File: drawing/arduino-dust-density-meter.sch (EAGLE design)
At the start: 7 parts

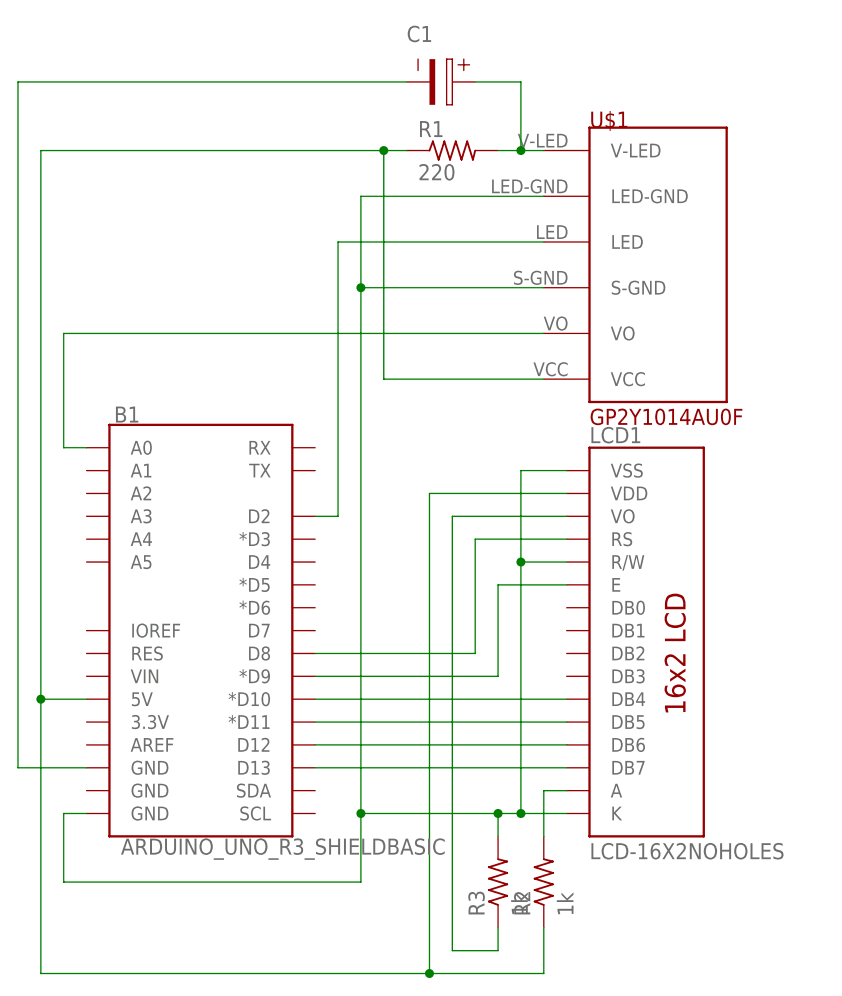
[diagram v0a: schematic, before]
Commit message: [DOCUMENT] Modify schematic for ease of viewing
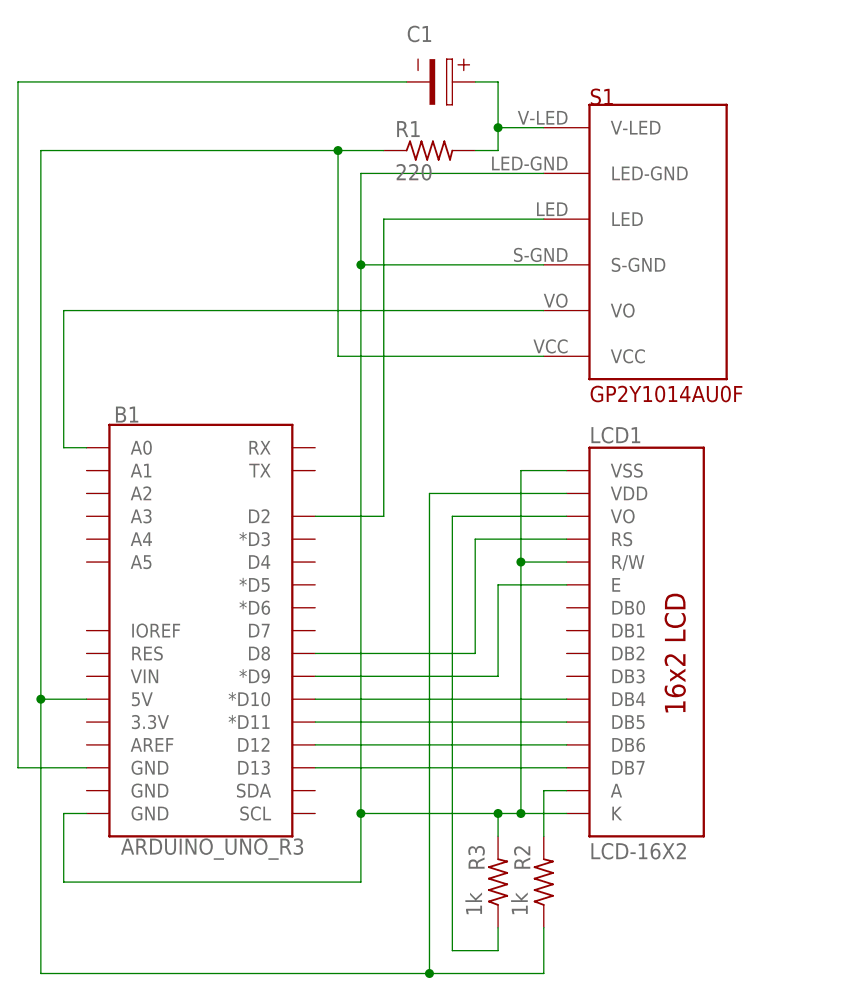
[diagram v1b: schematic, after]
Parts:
- removed U$1: GP2Y1014AU0F, sharp-dust-sensor:GP2Y1014AU0F
- added S1: GP2Y1014AU0F, sharp-dust-sensor:GP2Y1014AU0F
- B1: value ARDUINO_UNO_R3_SHIELDBASIC -> ARDUINO_UNO_R3
- LCD1: value LCD-16X2NOHOLES -> LCD-16X2
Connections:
- net N$1: now also S1.V-LED; no longer U$1.V-LED
- net N$2: now also S1.VCC; no longer U$1.VCC
- net N$4: now also S1.LED-GND, S1.S-GND; no longer U$1.LED-GND, U$1.S-GND
- net N$5: now also S1.LED; no longer U$1.LED
- net N$6: now also S1.VO; no longer U$1.VO
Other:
- moved on the sheet: R1
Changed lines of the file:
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@@
 </classes>
 <parts>
-<part name="B1" library="SparkFun-Boards" library_urn="urn:adsk.eagle:library:509" deviceset="ARDUINO_UNO_R3_SHIELD" device="BASIC" package3d_urn="urn:adsk.eagle:package:37321/1"/>
-<part name="U$1" library="sharp-dust-sensor" library_urn="urn:adsk.eagle:library:12467232" deviceset="GP2Y1014AU0F" device="" package3d_urn="urn:adsk.eagle:package:12467238/4"/>
+<part name="B1" library="SparkFun-Boards" library_urn="urn:adsk.eagle:library:509" deviceset="ARDUINO_UNO_R3_SHIELD" device="BASIC" package3d_urn="urn:adsk.eagle:package:37321/1" value="ARDUINO_UNO_R3"/>
+<part name="S1" library="sharp-dust-sensor" library_urn="urn:adsk.eagle:library:12467232" deviceset="GP2Y1014AU0F" device="" package3d_urn="urn:adsk.eagle:package:12467238/4"/>
 <part name="R1" library="BeagleBone_Black_Wireless" library_urn="urn:adsk.eagle:library:6644236" deviceset="R-US_" device="0309/12" package3d_urn="urn:adsk.eagle:package:8118473/1" value="220"/>
 <part name="C1" library="Wurth_Elektronik_Passive_Capacitors_rev18b" library_urn="urn:adsk.eagle:library:491551" deviceset="WCAP-PTG5" device="_870025575007" package3d_urn="urn:adsk.eagle:package:491745/2" technology="_10X12,5"/>
-<part name="LCD1" library="SparkFun-Displays" library_urn="urn:adsk.eagle:library:515" deviceset="LCD-16X2" device="NOHOLES" package3d_urn="urn:adsk.eagle:package:38513/1"/>
+<part name="LCD1" library="SparkFun-Displays" library_urn="urn:adsk.eagle:library:515" deviceset="LCD-16X2" device="NOHOLES" package3d_urn="urn:adsk.eagle:package:38513/1" value="LCD-16X2"/>
 <part name="R2" library="BeagleBone_Black_Wireless" library_urn="urn:adsk.eagle:library:6644236" deviceset="R-US_" device="0309/12" package3d_urn="urn:adsk.eagle:package:8118473/1" value="1k"/>
 <part name="R3" library="BeagleBone_Black_Wireless" library_urn="urn:adsk.eagle:library:6644236" deviceset="R-US_" device="0309/12" package3d_urn="urn:adsk.eagle:package:8118473/1" value="1k"/>
@@
 <attribute name="VALUE" x="105.41" y="12.446" size="1.778" layer="96" font="vector" align="top-left"/>
 </instance>
-<instance part="U$1" gate="G$1" x="165.1" y="76.2" smashed="yes">
-<attribute name="NAME" x="157.48" y="91.44" size="1.778" layer="94"/>
-<attribute name="VALUE" x="157.48" y="58.42" size="1.778" layer="94"/>
+<instance part="S1" gate="G$1" x="165.1" y="78.74" smashed="yes">
+<attribute name="NAME" x="157.48" y="93.98" size="1.778" layer="94"/>
+<attribute name="VALUE" x="157.48" y="60.96" size="1.778" layer="94"/>
 </instance>
-<instance part="R1" gate="G$1" x="142.24" y="88.9" smashed="yes">
-<attribute name="NAME" x="138.43" y="90.3986" size="1.778" layer="95"/>
-<attribute name="VALUE" x="138.43" y="85.598" size="1.778" layer="96"/>
+<instance part="R1" gate="G$1" x="139.7" y="88.9" smashed="yes">
+<attribute name="NAME" x="135.89" y="90.3986" size="1.778" layer="95"/>
+<attribute name="VALUE" x="135.89" y="85.598" size="1.778" layer="96"/>
 </instance>
 <instance part="C1" gate="G$1" x="139.7" y="96.52" smashed="yes" rot="R270">
@@
 </instance>
 <instance part="R2" gate="G$1" x="152.4" y="7.62" smashed="yes" rot="R90">
-<attribute name="NAME" x="150.9014" y="3.81" size="1.778" layer="95" rot="R90"/>
-<attribute name="VALUE" x="155.702" y="3.81" size="1.778" layer="96" rot="R90"/>
+<attribute name="NAME" x="150.9014" y="8.89" size="1.778" layer="95" rot="R90"/>
+<attribute name="VALUE" x="150.622" y="3.81" size="1.778" layer="96" rot="R90"/>
 </instance>
 <instance part="R3" gate="G$1" x="147.32" y="7.62" smashed="yes" rot="R90">
-<attribute name="NAME" x="145.8214" y="3.81" size="1.778" layer="95" rot="R90"/>
-<attribute name="VALUE" x="150.622" y="3.81" size="1.778" layer="96" rot="R90"/>
+<attribute name="NAME" x="145.8214" y="8.89" size="1.778" layer="95" rot="R90"/>
+<attribute name="VALUE" x="145.542" y="3.81" size="1.778" layer="96" rot="R90"/>
 </instance>
 </instances>
@@
 <net name="N$1" class="0">
 <segment>
+<pinref part="S1" gate="G$1" pin="V-LED"/>
+<wire x1="152.4" y1="91.44" x2="147.32" y2="91.44" width="0.1524" layer="91"/>
+<pinref part="C1" gate="G$1" pin="1"/>
+<wire x1="144.78" y1="96.52" x2="147.32" y2="96.52" width="0.1524" layer="91"/>
+<wire x1="147.32" y1="96.52" x2="147.32" y2="91.44" width="0.1524" layer="91"/>
 <pinref part="R1" gate="G$1" pin="2"/>
-<pinref part="U$1" gate="G$1" pin="V-LED"/>
-<wire x1="152.4" y1="88.9" x2="149.86" y2="88.9" width="0.1524" layer="91"/>
-<pinref part="C1" gate="G$1" pin="1"/>
-<wire x1="149.86" y1="88.9" x2="147.32" y2="88.9" width="0.1524" layer="91"/>
-<wire x1="144.78" y1="96.52" x2="149.86" y2="96.52" width="0.1524" layer="91"/>
-<wire x1="149.86" y1="96.52" x2="149.86" y2="88.9" width="0.1524" layer="91"/>
-<junction x="149.86" y="88.9"/>
+<wire x1="144.78" y1="88.9" x2="147.32" y2="88.9" width="0.1524" layer="91"/>
+<wire x1="147.32" y1="88.9" x2="147.32" y2="91.44" width="0.1524" layer="91"/>
+<junction x="147.32" y="91.44"/>
 </segment>
 </net>
@@
 <wire x1="99.06" y1="7.62" x2="132.08" y2="7.62" width="0.1524" layer="91"/>
 <wire x1="132.08" y1="7.62" x2="132.08" y2="15.24" width="0.1524" layer="91"/>
-<pinref part="U$1" gate="G$1" pin="LED-GND"/>
-<wire x1="132.08" y1="15.24" x2="132.08" y2="73.66" width="0.1524" layer="91"/>
-<wire x1="132.08" y1="73.66" x2="132.08" y2="83.82" width="0.1524" layer="91"/>
-<wire x1="132.08" y1="83.82" x2="152.4" y2="83.82" width="0.1524" layer="91"/>
-<pinref part="U$1" gate="G$1" pin="S-GND"/>
-<wire x1="152.4" y1="73.66" x2="132.08" y2="73.66" width="0.1524" layer="91"/>
-<junction x="132.08" y="73.66"/>
+<pinref part="S1" gate="G$1" pin="LED-GND"/>
+<wire x1="132.08" y1="15.24" x2="132.08" y2="76.2" width="0.1524" layer="91"/>
+<wire x1="132.08" y1="76.2" x2="132.08" y2="86.36" width="0.1524" layer="91"/>
+<wire x1="132.08" y1="86.36" x2="152.4" y2="86.36" width="0.1524" layer="91"/>
+<pinref part="S1" gate="G$1" pin="S-GND"/>
+<wire x1="152.4" y1="76.2" x2="132.08" y2="76.2" width="0.1524" layer="91"/>
+<junction x="132.08" y="76.2"/>
 <junction x="132.08" y="15.24"/>
 <pinref part="LCD1" gate="G$1" pin="R/W"/>
@@
 <net name="N$5" class="0">
 <segment>
-<pinref part="U$1" gate="G$1" pin="LED"/>
-<wire x1="152.4" y1="78.74" x2="129.54" y2="78.74" width="0.1524" layer="91"/>
-<wire x1="129.54" y1="78.74" x2="129.54" y2="48.26" width="0.1524" layer="91"/>
+<pinref part="S1" gate="G$1" pin="LED"/>
+<wire x1="152.4" y1="81.28" x2="134.62" y2="81.28" width="0.1524" layer="91"/>
+<wire x1="134.62" y1="81.28" x2="134.62" y2="48.26" width="0.1524" layer="91"/>
 <pinref part="B1" gate="G$1" pin="D2"/>
-<wire x1="129.54" y1="48.26" x2="127" y2="48.26" width="0.1524" layer="91"/>
+<wire x1="134.62" y1="48.26" x2="127" y2="48.26" width="0.1524" layer="91"/>
 </segment>
 </net>
 <net name="N$6" class="0">
 <segment>
-<pinref part="U$1" gate="G$1" pin="VO"/>
-<wire x1="152.4" y1="68.58" x2="99.06" y2="68.58" width="0.1524" layer="91"/>
-<wire x1="99.06" y1="68.58" x2="99.06" y2="55.88" width="0.1524" layer="91"/>
+<pinref part="S1" gate="G$1" pin="VO"/>
+<wire x1="152.4" y1="71.12" x2="99.06" y2="71.12" width="0.1524" layer="91"/>
+<wire x1="99.06" y1="71.12" x2="99.06" y2="55.88" width="0.1524" layer="91"/>
 <pinref part="B1" gate="G$1" pin="A0"/>
 <wire x1="99.06" y1="55.88" x2="101.6" y2="55.88" width="0.1524" layer="91"/>
@@
 <net name="N$2" class="0">
 <segment>
-<pinref part="U$1" gate="G$1" pin="VCC"/>
-<wire x1="152.4" y1="63.5" x2="134.62" y2="63.5" width="0.1524" layer="91"/>
+<pinref part="S1" gate="G$1" pin="VCC"/>
+<wire x1="152.4" y1="66.04" x2="129.54" y2="66.04" width="0.1524" layer="91"/>
 <pinref part="R1" gate="G$1" pin="1"/>
-<wire x1="137.16" y1="88.9" x2="134.62" y2="88.9" width="0.1524" layer="91"/>
-<wire x1="134.62" y1="88.9" x2="96.52" y2="88.9" width="0.1524" layer="91"/>
+<wire x1="134.62" y1="88.9" x2="129.54" y2="88.9" width="0.1524" layer="91"/>
+<wire x1="129.54" y1="88.9" x2="96.52" y2="88.9" width="0.1524" layer="91"/>
 <pinref part="B1" gate="G$1" pin="5V"/>
 <wire x1="96.52" y1="88.9" x2="96.52" y2="27.94" width="0.1524" layer="91"/>
 <wire x1="96.52" y1="27.94" x2="101.6" y2="27.94" width="0.1524" layer="91"/>
-<wire x1="134.62" y1="63.5" x2="134.62" y2="88.9" width="0.1524" layer="91"/>
-<junction x="134.62" y="88.9"/>
+<wire x1="129.54" y1="66.04" x2="129.54" y2="88.9" width="0.1524" layer="91"/>
+<junction x="129.54" y="88.9"/>
 <pinref part="R2" gate="G$1" pin="1"/>
 <wire x1="152.4" y1="2.54" x2="152.4" y2="-2.54" width="0.1524" layer="91"/>
